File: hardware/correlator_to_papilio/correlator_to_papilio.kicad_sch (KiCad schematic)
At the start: 2 parts, among them J1 Papilio Pro, U1 TART Correlator SODIMM

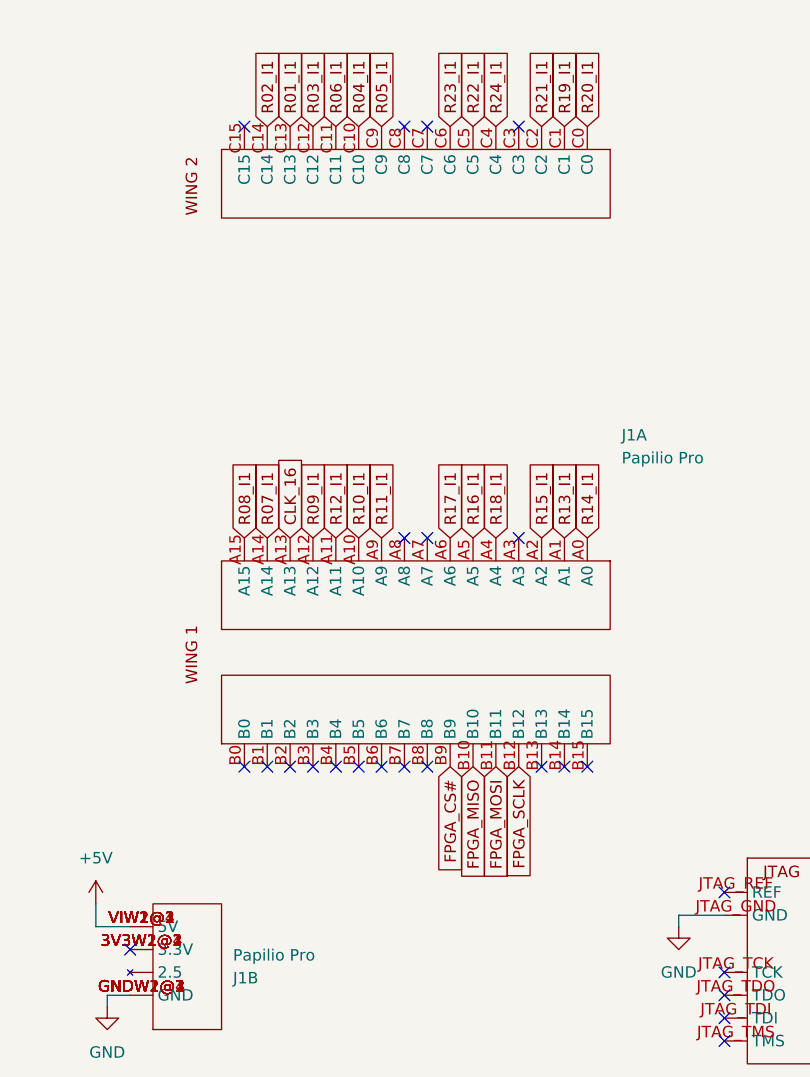
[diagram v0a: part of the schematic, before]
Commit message: Update the footprints and layout
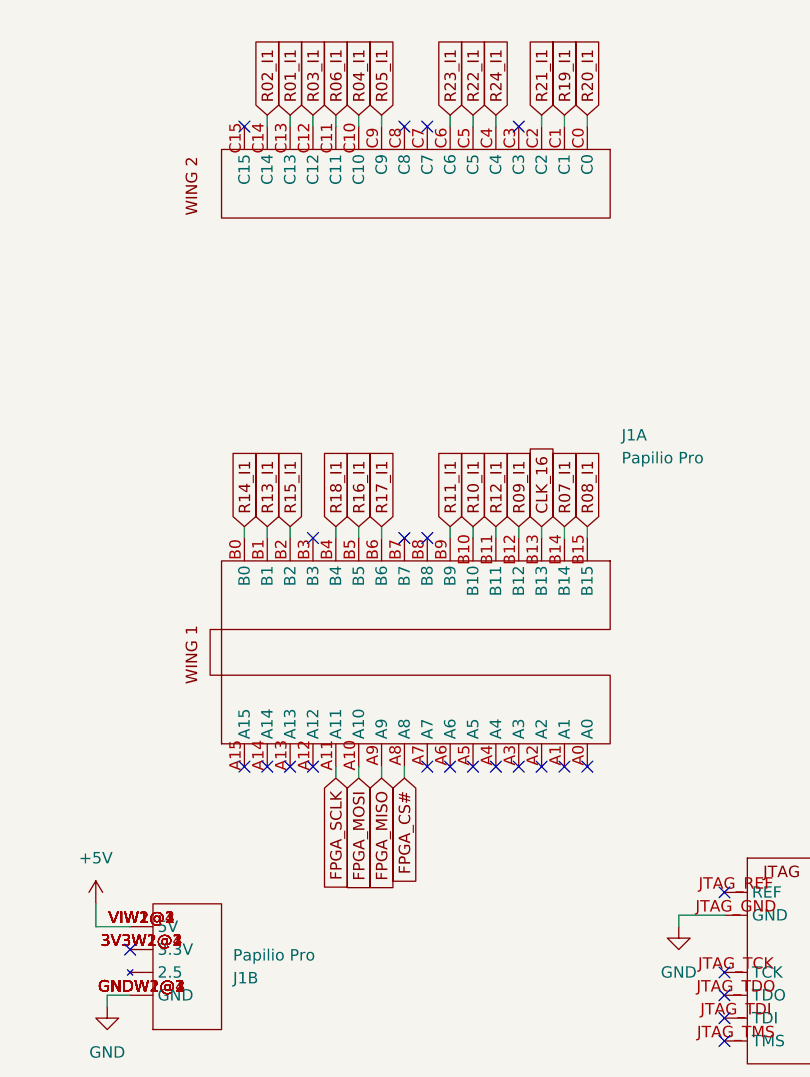
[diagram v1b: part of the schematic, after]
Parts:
- removed unit 3 of J1
- removed unit 2 of J1
- added unit 2 of J1
- added unit 3 of J1
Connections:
- net +5V: now also J1.VIW1@1 (5V), J1.VIW1@2 (5V), J1.VIW1@3 (5V), J1.VIW1@4 (5V), J1.VIW2@1 (5V), J1.VIW2@2 (5V)
- net CLK_16: now also J1.B13; no longer J1.A13
- net FPGA_CS#: now also J1.A8; no longer J1.B9
- net FPGA_MISO: now also J1.A9; no longer J1.B10
- net FPGA_MOSI: now also J1.A10; no longer J1.B11
- net FPGA_SCLK: now also J1.A11; no longer J1.B12
- net GND: now also J1.GNDW1@1 (GND), J1.GNDW1@2 (GND), J1.GNDW1@3 (GND), J1.GNDW1@4 (GND), J1.GNDW2@1 (GND), J1.GNDW2@2 (GND), J1.JTAG_GND (GND)
- net R07_I1: now also J1.B14; no longer J1.A14
- net R08_I1: now also J1.B15; no longer J1.A15
- net R09_I1: now also J1.B12; no longer J1.A12
- net R10_I1: now also J1.B10; no longer J1.A10
- net R11_I1: now also J1.B9; no longer J1.A9
- net R12_I1: now also J1.B11; no longer J1.A11
- net R13_I1: now also J1.B1; no longer J1.A1
- net R14_I1: now also J1.B0; no longer J1.A0
- net R15_I1: now also J1.B2; no longer J1.A2
- net R16_I1: now also J1.B5; no longer J1.A5
- net R17_I1: now also J1.B6; no longer J1.A6
- net R18_I1: now also J1.B4; no longer J1.A4
- new net: J1.3V3W1@1 (3.3V), J1.3V3W1@2 (3.3V), J1.3V3W1@3 (3.3V), J1.3V3W1@4 (3.3V), J1.3V3W2@1 (3.3V), J1.3V3W2@2 (3.3V)

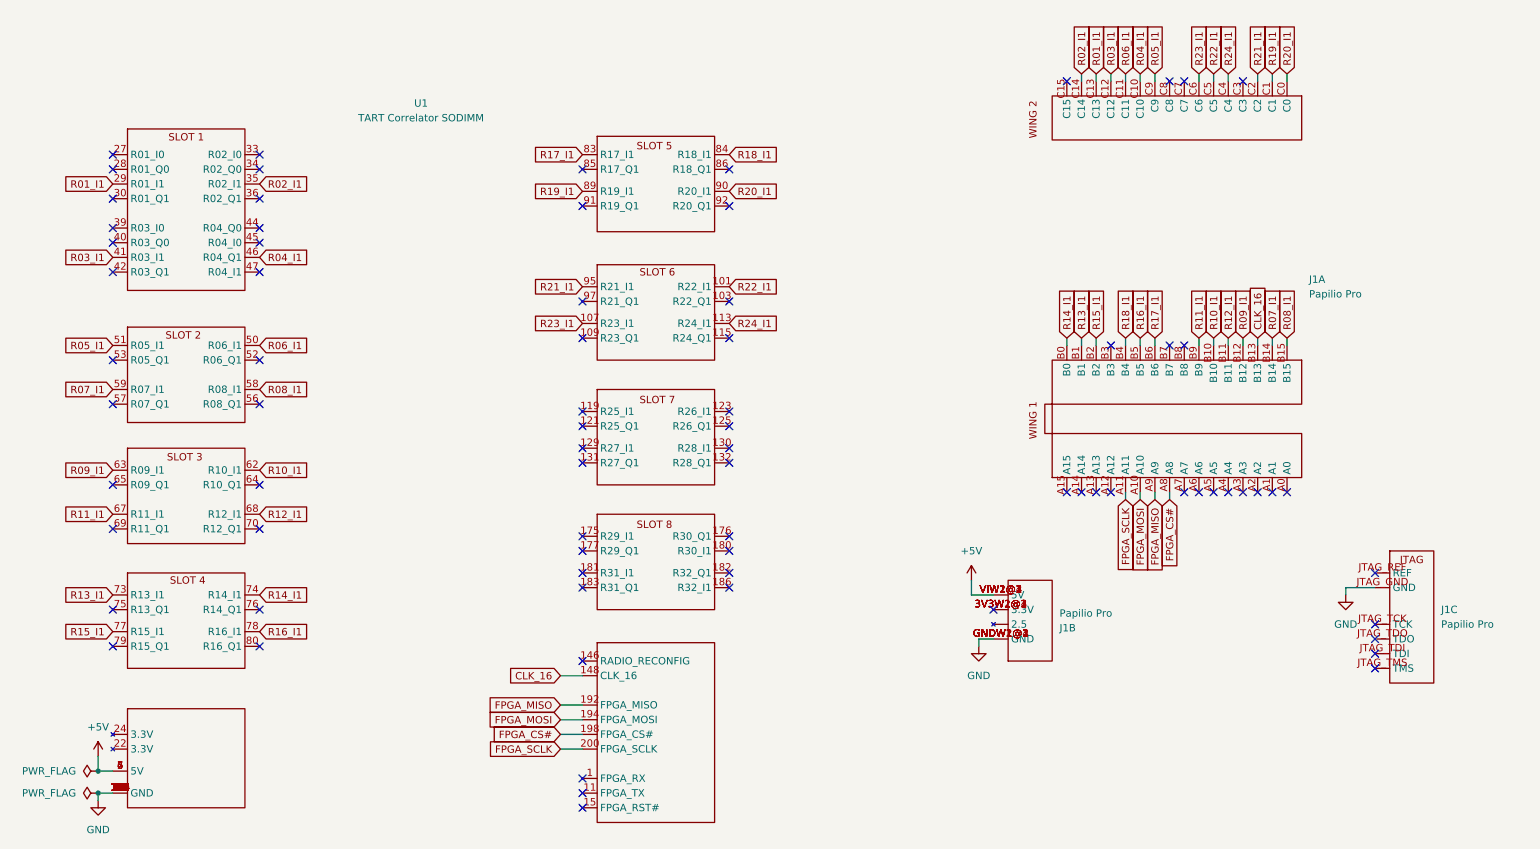
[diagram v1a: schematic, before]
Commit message: Fix radio 4, and radio 7 being on the wrong pins
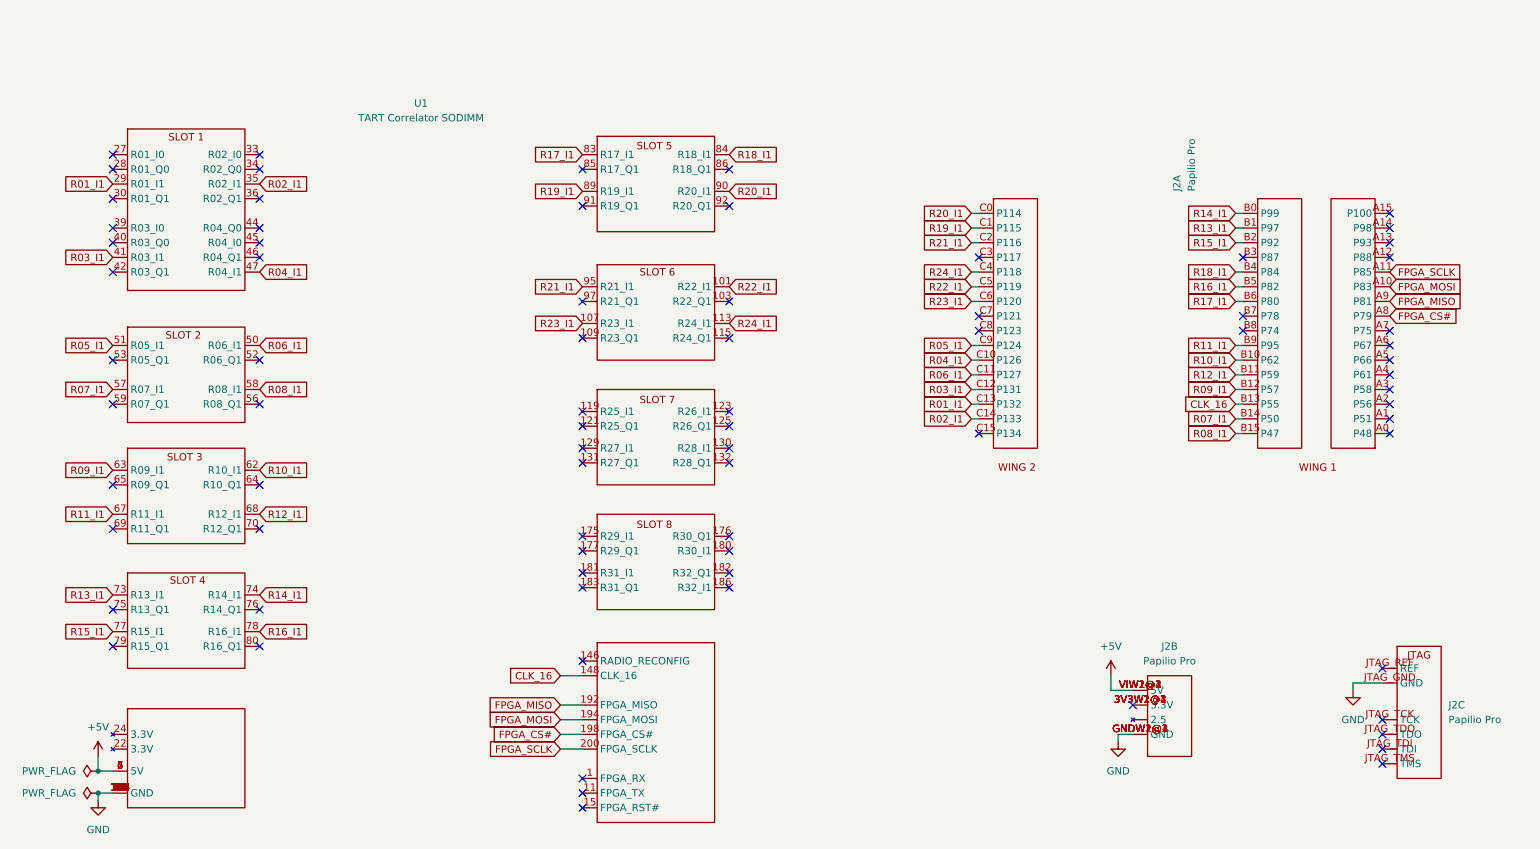
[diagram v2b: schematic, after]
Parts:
- removed J1: Papilio Pro, TART_Library:PAPILIO_PRO, symbol TART_Library:Papilio_Pro
- added J2: Papilio Pro, TART_Library:PAPILIO_PRO, symbol TART_Library:Papilio_Pro
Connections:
- net +5V: now also J2.VIW1@1 (5V), J2.VIW1@2 (5V), J2.VIW1@3 (5V), J2.VIW1@4 (5V), J2.VIW2@1 (5V), J2.VIW2@2 (5V)
- net CLK_16: now also J2.B13 (P55)
- net FPGA_CS#: now also J2.A8 (P79)
- net FPGA_MISO: now also J2.A9 (P81)
- net FPGA_MOSI: now also J2.A10 (P83)
- net FPGA_SCLK: now also J2.A11 (P85)
- net GND: now also J2.GNDW1@1 (GND), J2.GNDW1@2 (GND), J2.GNDW1@3 (GND), J2.GNDW1@4 (GND), J2.GNDW2@1 (GND), J2.GNDW2@2 (GND), J2.JTAG_GND (GND)
- net R01_I1: now also J2.C13 (P132)
- net R02_I1: now also J2.C14 (P133)
- net R03_I1: now also J2.C12 (P131)
- net R04_I1: now also U1.47 (R04_I1), J2.C10 (P126); no longer U1.46 (R04_Q1)
- net R05_I1: now also J2.C9 (P124)
- net R06_I1: now also J2.C11 (P127)
- net R07_I1: now also U1.57 (R07_I1), J2.B14 (P50); no longer U1.59 (R07_I1)
- net R08_I1: now also J2.B15 (P47)
- net R09_I1: now also J2.B12 (P57)
- net R10_I1: now also J2.B10 (P62)
- net R11_I1: now also J2.B9 (P95)
- net R12_I1: now also J2.B11 (P59)
- net R13_I1: now also J2.B1 (P97)
- net R14_I1: now also J2.B0 (P99)
- net R15_I1: now also J2.B2 (P92)
- net R16_I1: now also J2.B5 (P82)
- net R17_I1: now also J2.B6 (P80)
- net R18_I1: now also J2.B4 (P84)
- net R19_I1: now also J2.C1 (P115)
- net R20_I1: now also J2.C0 (P114)
- net R21_I1: now also J2.C2 (P116)
- net R22_I1: now also J2.C5 (P119)
- net R23_I1: now also J2.C6 (P120)
- net R24_I1: now also J2.C4 (P118)
- new net: J2.3V3W1@1 (3.3V), J2.3V3W1@2 (3.3V), J2.3V3W1@3 (3.3V), J2.3V3W1@4 (3.3V), J2.3V3W2@1 (3.3V), J2.3V3W2@2 (3.3V)
